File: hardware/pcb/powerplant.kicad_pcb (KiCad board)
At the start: 4 copper layers, 117.6 x 184 mm, 178 parts, among them J1 IDC-16_CONSOLE, J12 IDC-20_SWITCH_BUS, J13 IDC-12_SWITCH_ZONE_BUS, J14 IDC-10_SWITCH_LED_DATA, J15 IDC-6_ZONE_INFO_12V, J16 14_NIXIE_BUS, J17 J_AUDIO_OUT, J18 J_MIC, J19 J_LIGHT, J21 IDC-10_METER_SIG, J22 J_IN, J23 J_OUT, J24 POWER IN 12V, J6 RPi_GPIO, J7 IDC-34 METER_LED, Q1 IRLZ44N, Q2 IRLZ44N, Q3 IRLZ44N, Q4 IRLZ44N, Q5 IRLZ44N, Q6 IRLZ44N, U1 MCP4728, U10 LM358_DFN, U11 MCP23017_ML, U12 74AHCT125, U13 ULN2803A, U14 PCM5102A, U15 MCP23017_ML, U2 LM358_DFN, U3 LM358_DFN, U4 MCP4728, U5 ULN2803A, U6 74AHCT125, U7 74AHCT125, U8 ULN2803A, U9 MCP23017_ML

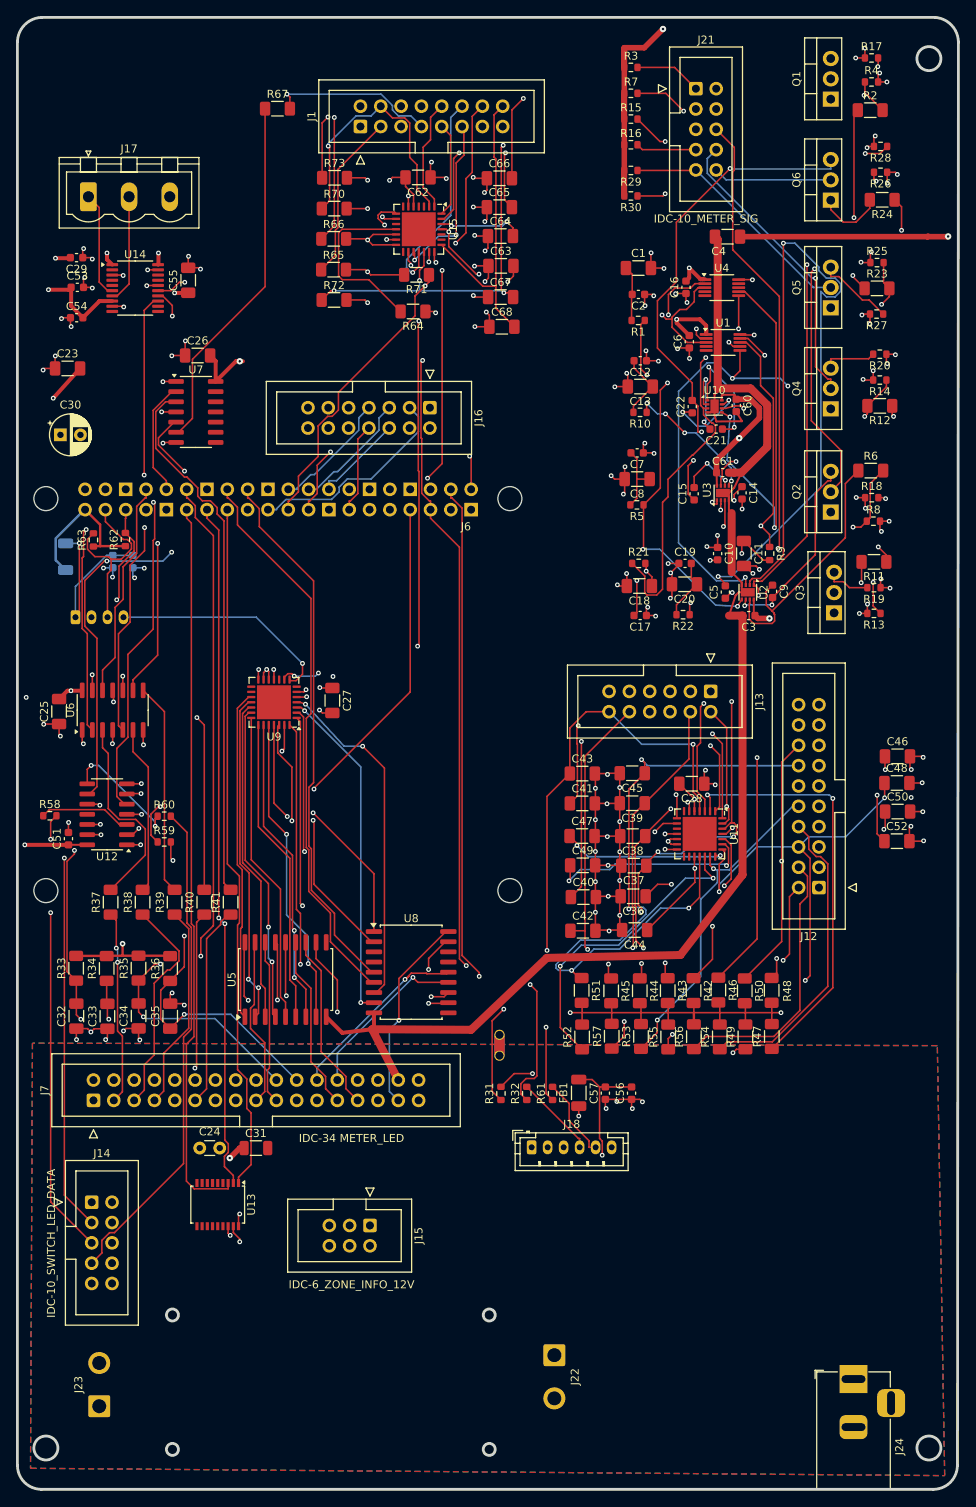
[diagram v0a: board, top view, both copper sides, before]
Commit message: Update hardware schematics and documentation; added source of truth for hardware, removed unused symbols, and modified connector specifications.
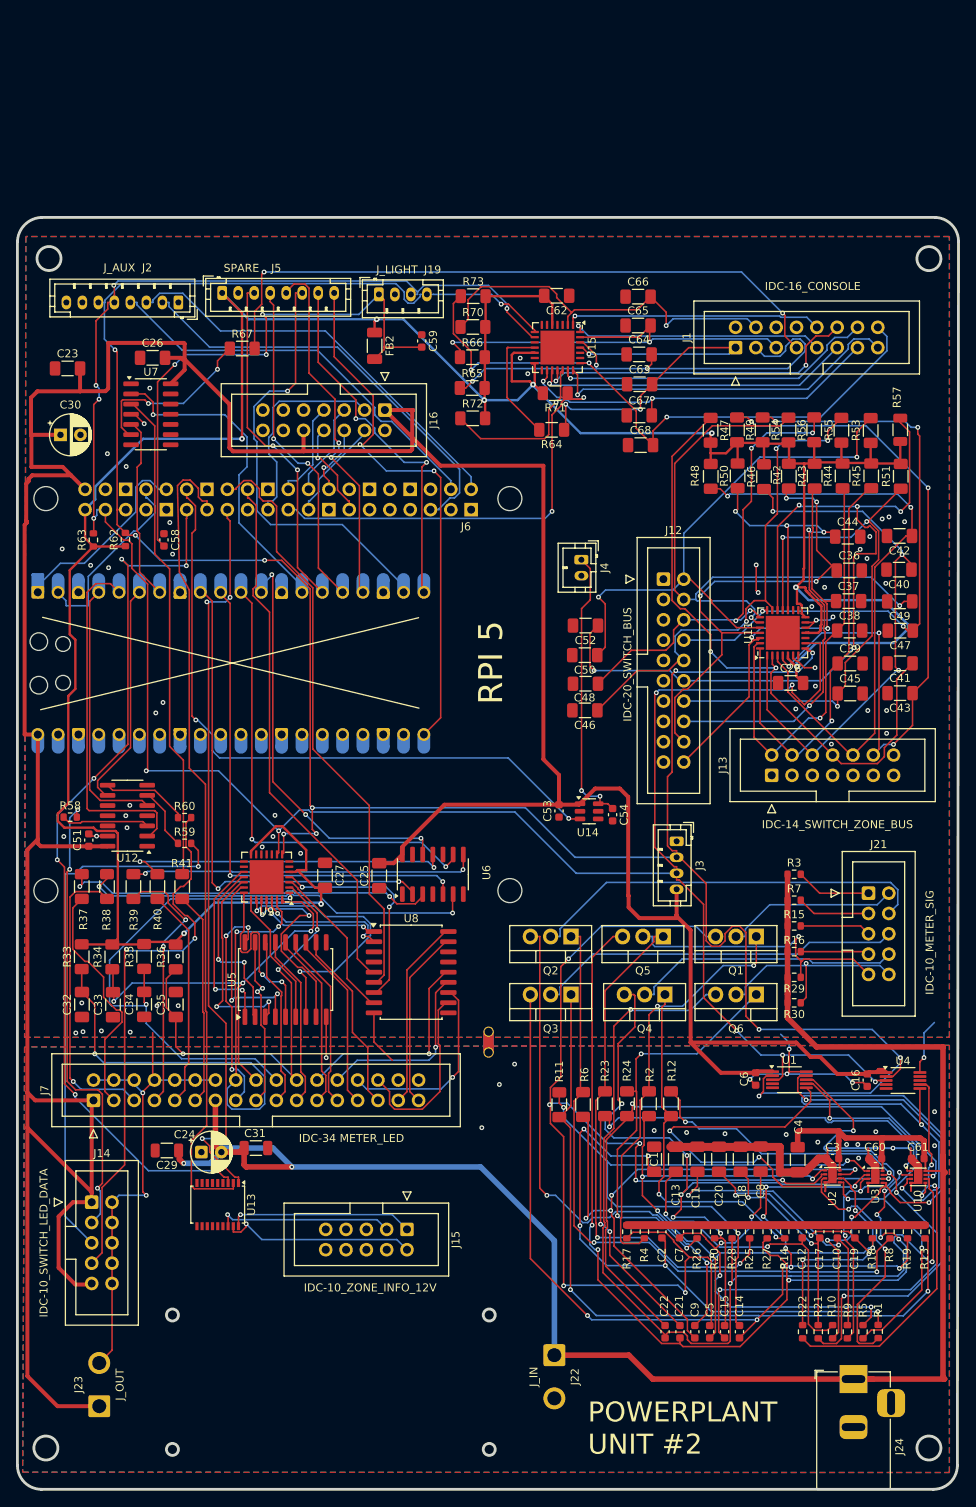
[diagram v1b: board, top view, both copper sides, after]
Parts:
- removed C55: 10 µF, Capacitor_SMD:C_1206_3216Metric_Pad1.33x1.80mm_HandSolder
- removed C56: 100 nF, Capacitor_SMD:C_0603_1608Metric
- removed C57: 1 µF, Capacitor_SMD:C_0603_1608Metric
- removed FB1: FerriteBead 600 Ω @ 100 MHz, Inductor_SMD:L_1206_3216Metric_Pad1.22x1.90mm_HandSolder
- removed J17: J_AUDIO_OUT, Connector_Phoenix_MSTB:PhoenixContact_MSTBVA_2,5_3-G-5,08_1x03_P5.08mm_Vertical
- removed J18: J_MIC, Connector_JST:JST_PH_B6B-PH-K_1x06_P2.00mm_Vertical
- removed R31, R32, R61: 33 Ω, Resistor_SMD:R_0603_1608Metric
- added A1: RaspberryPi_Pico, Module:RaspberryPi_Pico_Common_Unspecified, B.Cu at (42.2, 93.3)
- added J2: J_AUX, Connector_JST:JST_PH_B8B-PH-K_1x08_P2.00mm_Vertical, F.Cu at (35.6, 48.1)
- added J3: VL53L0X, Connector_JST:JST_PH_B4B-PH-K_1x04_P2.00mm_Vertical, F.Cu at (97.9, 115.5)
- added J4: J_LCD_PWR, Connector_JST:JST_PH_B2B-PH-K_1x02_P2.00mm_Vertical, F.Cu at (86.0, 80.3)
- added J5: SPARE, Connector_JST:JST_PH_B8B-PH-K_1x08_P2.00mm_Vertical, F.Cu at (41.1, 47.0)
- C24: footprint Capacitor_THT:C_Disc_D3.0mm_W1.6mm_P2.50mm -> Capacitor_THT:CP_Radial_D5.0mm_P2.50mm
- C29: value 100 nF -> 10 µF; footprint Capacitor_SMD:C_0603_1608Metric -> Resistor_SMD:R_1206_3216Metric
- C53: value 100 nF -> 1 µF
- C54: value 100 nF -> 4.7 µF
- C58, C59, FB2, J19: moved to F.Cu
- J13: value IDC-12_SWITCH_ZONE_BUS -> IDC-14_SWITCH_ZONE_BUS; footprint Connector_IDC:IDC-Header_2x06_P2.54mm_Vertical -> Connector_IDC:IDC-Header_2x07_P2.54mm_Vertical
- J15: value IDC-6_ZONE_INFO_12V -> IDC-10_ZONE_INFO_12V; footprint Connector_IDC:IDC-Header_2x03_P2.54mm_Vertical -> Connector_IDC:IDC-Header_2x05_P2.54mm_Vertical
- R52: footprint Resistor_SMD:R_1206_3216Metric_Pad1.30x1.75mm_HandSolder -> Resistor_SMD:R_1206_3216Metric
- U14: value PCM5102A -> TPS22917DBV; footprint Package_SO:TSSOP-20_4.4x6.5mm_P0.65mm -> Package_TO_SOT_SMD:SOT-23-6
- moved R17 149.9 mm to (91.7, 164.3), turned to -90 degrees
- moved R4 146.5 mm to (93.9, 164.3), turned to 90 degrees
- moved R28 136.9 mm to (104.8, 164.3), turned to 90 degrees
- moved R26 134.4 mm to (100.5, 164.3), turned to -90 degrees
- moved R1 129.9 mm to (123.1, 176.8), turned to 90 degrees
- moved R2 127.2 mm to (94.5, 148.3), turned to 90 degrees
- moved R25 122.2 mm to (107.0, 164.3), turned to -90 degrees
- moved R10 117.4 mm to (117.4, 176.8), turned to 90 degrees
- moved R24 117.4 mm to (91.7, 148.3), turned to 90 degrees
- moved C2 117.2 mm to (96.1, 164.3), turned to -90 degrees
- moved C4 115.7 mm to (113.0, 155.3), turned to -90 degrees
- moved C22 115.7 mm to (96.5, 176.8), turned to -90 degrees
- moved R27 115.5 mm to (109.2, 164.3), turned to 90 degrees
- moved C21 112.9 mm to (98.3, 176.8), turned to -90 degrees
- moved C29 112.2 mm to (34.2, 154.2)
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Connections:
- net /I2C_SCL renamed /AUX_SCL
- net /I2C_SDA renamed /AUX_SDA
- C1 pad 2: GND -> GNDPWR
- C10 pad 1: GND -> GNDPWR
- C11 pad 2: GND -> GNDPWR
- C12 pad 1: GND -> GNDPWR
- C13 pad 2: GND -> GNDPWR
- C17 pad 1: GND -> GNDPWR
- C18 pad 2: GND -> GNDPWR
- C19 pad 1: GND -> GNDPWR
- C2 pad 1: GND -> GNDPWR
- C20 pad 2: GND -> GNDPWR
- C29 pad 1: GND -> +12V
- C29 pad 2: +5V -> GNDPWR
- C53 pad 1: +5V -> GND
- C53 pad 2: GND -> +5V
- C54 pad 1: GND -> Net-(J4-Pin_1)
- C54 pad 2: +5V -> GND
- C7 pad 1: GND -> GNDPWR
- C8 pad 2: GND -> GNDPWR
- J23 pad 2: GNDPWR -> GND
- J6 pad 10: /GPIO_LED5 -> /GP0_TX_PICO
- J6 pad 12: /I2S_BCK -> /LCD_PWR_EN
- J6 pad 29: /GPIO_LED2 -> unconnected-(J6-BCM5-Pad29)
- J6 pad 31: /GPIO_LED3 -> unconnected-(J6-BCM6-Pad31)
- J6 pad 32: /LED_RANGE_DATA_IN -> unconnected-(J6-BCM12_PWM0-Pad32)
- J6 pad 33: /LED_MODE_DATA_IN -> unconnected-(J6-BCM13_PWM1-Pad33)
- J6 pad 35: /I2S_LRCK -> /AUX_I2S_LRCLK
- J6 pad 36: /LED_TEMP_DATA_IN -> unconnected-(J6-BCM16-Pad36)
- J6 pad 37: /GPIO_VOL_RING -> unconnected-(J6-BCM26-Pad37)
- J6 pad 38: /MIC_I2S_DOUT -> /AUX_I2S_RX
- J6 pad 40: /I2S_DIN -> /AUX_I2S_TX
- J6 pad 7: /GPIO_LED1 -> unconnected-(J6-BCM4_GPCLK0-Pad7)
- J6 pad 8: /GPIO_LED4 -> /GP1_RX_PICO
- NT1 pad 1: GNDPWR -> GND
- NT1 pad 2: GND -> GNDPWR
- R13 pad 2: GND -> GNDPWR
- R14 pad 2: GND -> GNDPWR
- R17 pad 1: GND -> GNDPWR
- R18 pad 1: GND -> GNDPWR
- R19 pad 1: GND -> GNDPWR
- R20 pad 1: GND -> GNDPWR
- R25 pad 1: GND -> GNDPWR
- R26 pad 1: GND -> GNDPWR
- R27 pad 2: GND -> GNDPWR
- R28 pad 2: GND -> GNDPWR
- R4 pad 2: GND -> GNDPWR
- R8 pad 2: GND -> GNDPWR
- U12 pad 2: /LED_MODE_DATA_IN -> /BLK_SWITCH_LED/LED_MODE_DATA_IN
- U12 pad 5: /LED_RANGE_DATA_IN -> /BLK_SWITCH_LED/LED_RANGE_DATA_IN
- U12 pad 9: /LED_TEMP_DATA_IN -> /BLK_SWITCH_LED/LED_TEMP_DATA_IN
- U14 pad 2: unconnected-(U14-CAPP-Pad2) -> GND
- U14 pad 3: GND -> /LCD_PWR_EN
- U14 pad 6: Net-(J17-Pin_1) -> Net-(J4-Pin_1)
- U6 pad 12: /GPIO_LED4 -> /BLK_METER_LED/GPIO_LED4
- U6 pad 2: /GPIO_LED1 -> /BLK_METER_LED/GPIO_LED1
- U6 pad 5: /GPIO_LED2 -> /BLK_METER_LED/GPIO_LED2
- U6 pad 9: /GPIO_LED3 -> /BLK_METER_LED/GPIO_LED3
- U7 pad 2: /GPIO_LED5 -> /BLK_METER_LED/GPIO_LED5
- U7 pad 5: /GPIO_VOL_RING -> /BLK_METER_LED/GPIO_VOL_RING
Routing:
- net +12V: track 442.9 -> 262.5 mm, vias 5 -> 2
- net GND: track 271.6 -> 109.9 mm, vias 149 -> 56
- net /I2S_BCK: track 142.4 -> 0.00 mm, vias 3 -> 0
- net /I2S_LRCK: track 141.2 -> 0.00 mm, vias 4 -> 0
- net /AUX_SCL: track 205.9 -> 325.6 mm, vias 8 -> 12
- net /SENSE_C: track 26.3 -> 120.9 mm, vias 2 -> 9
- net +3.3V: track 483.9 -> 392.1 mm, vias 16 -> 9
- net /LCD_PWR_EN: track 0.00 -> 84.1 mm, vias 0 -> 2
- net /MIC_I2S_DOUT: track 82.9 -> 0.00 mm, vias 2 -> 0
- net Net-(Q3-G): track 13.8 -> 92.2 mm
- net /SENSE_E1: track 42.1 -> 119.8 mm, vias 2 -> 8
- net /LED_TEMP_DATA_IN: track 76.6 -> 0.00 mm, vias 2 -> 0
- net /AUX_SDA: track 235.1 -> 308.7 mm, vias 7 -> 12
- net GNDPWR: track 174.8 -> 102.7 mm, vias 0 -> 16
- net /LED_RANGE_DATA_IN: track 71.0 -> 0.00 mm, vias 1 -> 0
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- added copper zone on B.Cu, net GND
- added copper zone on F.Cu, net GND
- removed copper zone on In1.Cu, net +5V
- removed copper zone on In2.Cu, net GND
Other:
- board size 117.6 x 184 mm -> 117.6 x 159 mm
- copper layers 4 -> 2
- board text added: "POWERPLANT UNIT #2"
- board text added: "RPI 5"
- board text added: "RPI NANO 2H"
